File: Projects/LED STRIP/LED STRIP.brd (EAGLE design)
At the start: 406.4 x 25.4 mm, 70 parts, among them U1 PCA9635, U2 PCA9635, U3 PCA9635

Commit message: lowered LED bias, changed order of LEDs to accommodate routing
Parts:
- moved LED13 162.5 mm to (292.0, 12.7)
- moved LED14 162.5 mm to (271.7, 12.7)
- moved LED4 162.5 mm to (149.9, 12.7)
- moved LED5 162.5 mm to (129.6, 12.7)
- moved R11 162.5 mm to (169.0, 2.54)
- moved R19 162.5 mm to (105.5, 2.54)
- moved R27 162.5 mm to (394.9, 2.54)
- moved R3 162.5 mm to (232.5, 2.54)
- moved R32 162.5 mm to (351.7, 2.54)
- moved R35 162.5 mm to (331.4, 2.54)
- moved R43 162.5 mm to (267.9, 2.54)
- moved R8 162.5 mm to (189.3, 2.54)
- moved LED0 162.5 mm to (231.2, 12.7)
- moved LED1 162.5 mm to (210.9, 12.7)
- moved LED10 162.5 mm to (353.0, 12.7)
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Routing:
- net RED4: track 32.6 -> 42.1 mm
- net RED3: track 32.3 -> 41.8 mm
- net RED9: track 33.0 -> 42.5 mm
- net BLUE0: track 21.0 -> 30.5 mm
- net RED10: track 32.9 -> 42.4 mm
- net GREEN7: track 27.4 -> 36.9 mm
- net BLUE15: track 21.3 -> 30.8 mm
- net RED5: track 32.8 -> 42.3 mm
- net GREEN5: track 26.9 -> 36.4 mm
- net GREEN0: track 27.1 -> 36.6 mm
- net BLUE1: track 20.8 -> 30.3 mm
- net GREEN4: track 26.7 -> 36.2 mm
- net GREEN12: track 27.0 -> 36.5 mm
- net BLUE8: track 21.4 -> 30.9 mm
- net BLUE5: track 21.0 -> 30.5 mm
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
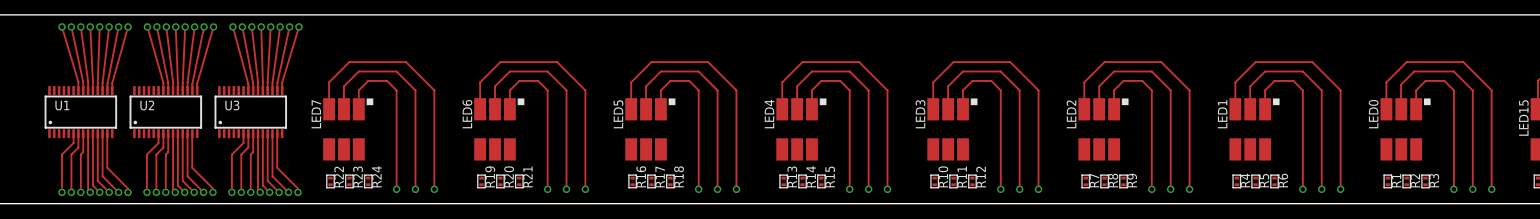
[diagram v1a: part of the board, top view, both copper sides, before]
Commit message: green and blue wired
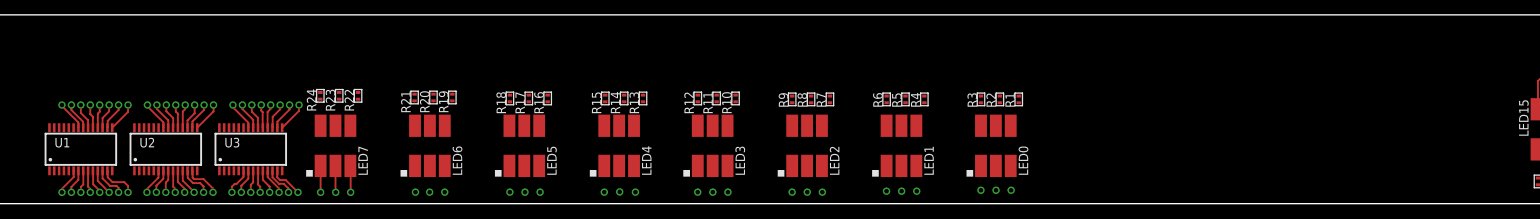
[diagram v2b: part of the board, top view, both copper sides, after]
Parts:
- moved R3 61.0 mm to (172.7, 14.5), turned to 270 degrees
- moved LED0 59.0 mm to (172.7, 5.08), turned to 90 degrees
- moved R2 56.0 mm to (175.2, 14.5), turned to 270 degrees
- moved R6 53.5 mm to (160.0, 14.5), turned to 270 degrees
- moved LED1 51.5 mm to (160.0, 5.08), turned to 90 degrees
- moved R1 51.1 mm to (177.7, 14.5), turned to 270 degrees
- moved R5 48.6 mm to (162.5, 14.5), turned to 270 degrees
- moved R9 46.1 mm to (147.3, 14.5), turned to 270 degrees
- moved LED2 44.0 mm to (147.3, 5.08), turned to 90 degrees
- moved R4 43.7 mm to (165.0, 14.5), turned to 270 degrees
- moved R8 41.3 mm to (149.8, 14.5), turned to 270 degrees
- moved R12 38.9 mm to (134.6, 14.6), turned to 270 degrees
- moved LED3 36.5 mm to (134.6, 5.08), turned to 90 degrees
- moved R7 36.4 mm to (152.3, 14.5), turned to 270 degrees
- moved R11 34.1 mm to (137.1, 14.6), turned to 270 degrees
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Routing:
- net GREEN0: track 36.6 -> 122.2 mm
- net BLUE0: track 30.5 -> 109.2 mm
- net GREEN1: track 36.2 -> 107.6 mm
- net BLUE1: track 30.3 -> 94.3 mm
- net GREEN2: track 35.9 -> 93.0 mm
- net BLUE2: track 30.0 -> 79.6 mm
- net GREEN3: track 35.9 -> 78.8 mm
- net RED4: track 42.1 -> 3.27 mm
- net RED5: track 42.3 -> 3.53 mm
- net RED1: track 42.1 -> 3.29 mm
- net RED2: track 41.8 -> 3.03 mm
- net RED0: track 42.3 -> 3.55 mm
- net RED3: track 41.8 -> 3.03 mm
- net RED6: track 42.6 -> 4.30 mm
- net BLUE3: track 30.0 -> 64.9 mm
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
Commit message: all traces for LED0-LED7 routed
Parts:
- moved R49 3.31 mm to (29.0, 15.7)
- moved R50 2.79 mm to (24.1, 16.3)
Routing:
- net RED0: track 3.55 -> 139.0 mm
- net RED1: track 3.29 -> 124.4 mm
- net RED2: track 3.03 -> 109.7 mm
- net RED3: track 3.03 -> 95.1 mm
- net RED4: track 3.27 -> 81.1 mm
- net RED5: track 3.53 -> 66.9 mm
- net RED6: track 4.30 -> 53.3 mm
- net RED7: track 8.54 -> 39.5 mm
- net N$23: track 0.00 -> 4.01 mm
- net N$25: track 0.00 -> 3.79 mm
- net N$26: track 0.00 -> 3.77 mm
- net N$30: track 0.00 -> 3.73 mm
- net N$27: track 0.00 -> 3.70 mm
- net N$33: track 0.00 -> 3.67 mm
- net N$20: track 0.00 -> 3.60 mm
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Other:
- board size 406.4 x 25.4 mm -> 406.4 x 19.1 mm

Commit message: LED8-15 placed .9" spacing
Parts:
- moved LED0 71.1 mm to (243.8, 5.08)
- moved R1 71.1 mm to (248.9, 14.5)
- moved R2 71.1 mm to (246.3, 14.5)
- moved R3 71.1 mm to (243.8, 14.5)
- moved R4 61.0 mm to (226.0, 14.5)
- moved R5 61.0 mm to (223.5, 14.5)
- moved LED1 61.0 mm to (220.9, 5.08)
- moved R6 61.0 mm to (220.9, 14.5)
- moved LED2 50.8 mm to (198.1, 5.08)
- moved R9 50.8 mm to (198.1, 14.5)
- moved R7 50.8 mm to (203.1, 14.5)
- moved R8 50.8 mm to (200.6, 14.5)
- moved R25 43.7 mm to (431.9, 14.7), turned to 270 degrees
- moved R28 41.3 mm to (409.0, 14.7), turned to 270 degrees
- moved R10 40.6 mm to (180.3, 14.6)
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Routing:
- net BLUE8: track 26.0 -> 355.1 mm
- net GREEN0: track 125.5 -> 196.6 mm
- net RED0: track 139.0 -> 210.1 mm
- net BLUE0: track 112.5 -> 183.6 mm
- net RED1: track 124.4 -> 185.3 mm
- net GREEN1: track 111.0 -> 172.0 mm
- net BLUE1: track 97.7 -> 158.7 mm
- net BLUE2: track 83.1 -> 133.9 mm
- net RED2: track 109.7 -> 160.5 mm
- net GREEN2: track 96.6 -> 147.4 mm
- net RED3: track 95.1 -> 135.8 mm
- net GREEN3: track 82.3 -> 123.0 mm
- net BLUE3: track 68.4 -> 109.0 mm
- net RED15: track 38.4 -> 3.97 mm
- net RED9: track 37.5 -> 3.68 mm
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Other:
- board size 406.4 x 19.1 mm -> 444.5 x 19.1 mm

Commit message: all LEDs wired to ICs
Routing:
- net RED8: track 3.94 -> 382.6 mm
- net GREEN8: track 3.96 -> 368.9 mm
- net RED9: track 3.68 -> 361.8 mm
- net GREEN9: track 3.71 -> 347.3 mm
- net RED10: track 3.42 -> 339.6 mm
- net BLUE9: track 3.74 -> 333.1 mm
- net GREEN10: track 3.45 -> 325.8 mm
- net RED11: track 3.16 -> 316.9 mm
- net BLUE10: track 3.48 -> 311.2 mm
- net GREEN11: track 3.19 -> 303.6 mm
- net RED12: track 3.20 -> 296.0 mm
- net BLUE11: track 3.23 -> 289.6 mm
- net GREEN12: track 3.17 -> 283.0 mm
- net RED13: track 3.46 -> 274.8 mm
- net BLUE12: track 3.14 -> 267.9 mm
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
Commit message: relocated resistors
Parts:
- moved R50 19.8 mm to (43.7, 13.0)
- moved R49 17.5 mm to (46.2, 13.0)
- moved R15 17.2 mm to (169.4, 10.5)
- moved R33 17.2 mm to (397.8, 10.6)
- moved R21 17.1 mm to (123.1, 10.4)
- moved R42 17.0 mm to (329.0, 10.6)
- moved R45 17.0 mm to (306.1, 10.6)
- moved R24 16.9 mm to (100.0, 10.4)
- moved R12 16.8 mm to (191.5, 10.5)
- moved R3 16.8 mm to (260.0, 10.4)
- moved R30 16.8 mm to (420.2, 10.6)
- moved R39 16.8 mm to (351.7, 10.7)
- moved R18 16.5 mm to (145.6, 10.5)
- moved R36 16.5 mm to (374.2, 10.6)
- moved R48 16.5 mm to (282.7, 10.6)
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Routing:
- net N$18: track 0.00 -> 20.3 mm
- net N$28: track 0.00 -> 15.0 mm
- net N$21: track 0.00 -> 9.87 mm
- net N$23: track 4.01 -> 0.09 mm
- net N$26: track 3.77 -> 0.00 mm
- net N$25: track 3.79 -> 0.05 mm
- net N$30: track 3.73 -> 0.00 mm
- net N$27: track 3.70 -> 0.00 mm
- net N$33: track 3.67 -> 0.00 mm
- net N$22: track 3.55 -> 0.00 mm
- net N$41: track 3.55 -> 0.00 mm
- net N$38: track 3.55 -> 0.00 mm
- net N$42: track 3.55 -> 0.00 mm
- net N$20: track 3.60 -> 0.06 mm
- net N$16: track 3.53 -> 0.00 mm
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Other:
- board size 444.5 x 19.1 mm -> 444.5 x 17.8 mm

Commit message: resistors wired
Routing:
- net N$45: track 0.00 -> 21.3 mm
- net N$24: track 0.00 -> 21.2 mm
- net N$15: track 0.00 -> 21.0 mm
- net N$12: track 0.00 -> 21.0 mm
- net N$29: track 0.00 -> 20.9 mm
- net N$39: track 0.00 -> 20.8 mm
- net N$48: track 0.00 -> 20.8 mm
- net N$6: track 0.00 -> 20.8 mm
- net N$9: track 0.00 -> 20.6 mm
- net N$20: track 0.06 -> 20.7 mm
- net N$32: track 0.00 -> 20.6 mm
- net N$36: track 0.00 -> 20.4 mm
- net N$44: track 0.00 -> 20.3 mm
- net N$3: track 0.00 -> 20.3 mm
- net N$35: track 0.00 -> 20.1 mm
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
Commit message: changed board size (shifted everything to the left)
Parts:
- moved R49 19.8 mm to (26.4, 12.2)
- moved R50 19.8 mm to (23.9, 12.2)
- moved R33 18.8 mm to (379.0, 10.9)
- moved R35 18.8 mm to (352.9, 10.9)
- moved LED4 18.8 mm to (133.7, 5.33)
- moved R14 18.8 mm to (148.0, 10.8)
- moved R4 18.8 mm to (213.0, 10.7)
- moved R9 18.8 mm to (195.3, 10.7)
- moved LED6 18.8 mm to (87.9, 5.33)
- moved R18 18.8 mm to (126.8, 10.8)
- moved R20 18.8 mm to (101.8, 10.7)
- moved R23 18.8 mm to (78.7, 10.6)
- moved R24 18.8 mm to (81.2, 10.6)
- moved U1 18.8 mm to (32.8, 7.57)
- moved U2 18.8 mm to (44.2, 7.57)
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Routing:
- net +5V: track 0.00 -> 594.3 mm
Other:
- board size 444.5 x 17.8 mm -> 431.8 x 19.1 mm
